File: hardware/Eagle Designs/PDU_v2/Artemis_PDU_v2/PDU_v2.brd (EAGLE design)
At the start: 160 x 100 mm, 101 parts, among them T1 2N5088, U1 DRV8847PWPR, U10 PE014006, U11 IRLML2803PBFCT-ND, U12 IRLML2803PBFCT-ND, U2 DRV8847PWPR, U3 LTC1477CS8LINEAR_TECHNOLOGY_L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, U4 LTC1477CS8LINEAR_TECHNOLOGY_L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, U5 LTC1477CS8LINEAR_TECHNOLOGY_L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, U6 LTC1477CS8LINEAR_TECHNOLOGY_L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, U7 LTC1477CS8LINEAR_TECHNOLOGY_L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, U8 LTC1477CS8LINEAR_TECHNOLOGY_L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, U9 LTC1477CS8LINEAR_TECHNOLOGY_L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

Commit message: updated PDU v2 Eagle files and Artemis Library
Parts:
- added C1, C2: 22uF, HSFL_Main_Library:0805
- added C3, C45, C51: 0.1uF, HSFL_Main_Library:0805
- added C4, C44: 1uF, HSFL_Main_Library:0805
- added C43, C47, C48: 4.7uF, HSFL_Main_Library:0805
- added C46, C49: 10uF, HSFL_Main_Library:0805
- added C50: 0.47uF, HSFL_Main_Library:0805
- added C52: 100pF, HSFL_Main_Library:0805
- added C53: 4.7nF, HSFL_Main_Library:0805
- added C74, C75, C76, C77, C78, C79, C80, C81: 33uF, HSFL_Main_Library:1206
- added D4: (no value), adafruit:SOD-123FL
- added L5: 6uH, HSFL_Main_Library:7443551600
- added M1, M2: BSZ100N06LS3, HSFL_Main_Library:BSZ100N06LS3
- added M3, M4: BSZ033NE2LS5, HSFL_Main_Library:BSZ100N06LS3
- added R1: 4m, HSFL_Main_Library:0805
- added R2: 390K, HSFL_Main_Library:0805
- added R3: 180K, HSFL_Main_Library:0805
- added R30, R32: 10K, HSFL_Main_Library:0805
- added R31: 27K, HSFL_Main_Library:0805
- added R33, R6: 100K, HSFL_Main_Library:0805
- added R4: 15m, HSFL_Main_Library:0805
- added R46: 510K, HSFL_Main_Library:0805
- added R47: 270K, HSFL_Main_Library:0805
- added R5: 130K, HSFL_Main_Library:0805
- added U13: LT8390EFE#PBF, Artemis:SOP65P640X120-29N
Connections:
- new net N$1: C3.1, M1.P$2, M1.P$3, M1.P$4, M2.P$5, M2.P$6, M2.P$7, M2.P$8, M2.P$9, R1.2, U13.3, U13.5
- new net N$2: C3.2, U13.2
- new net N$3: M2.P$1, U13.1
- new net N$38: C52.1, R31.2, U13.20
- new net N$39: C50.1, U13.11, U13.12, U13.13
- new net N$4: M1.P$1, U13.4
- new net N$40: R32.2, R5.1
- new net N$41: C45.1, L5.P$2, M3.P$5, M3.P$6, M3.P$7, M3.P$8, M3.P$9, M4.P$2, M4.P$3, M4.P$4, U13.26
- new net N$42: U13.23
- new net N$43: R6.1, U13.17
- new net N$44: C43.1, R6.2, U13.8
- new net N$45: L5.P$1, R1.1, U13.6
- new net N$47: C45.2, U13.27
- new net N$48: C44.1, C46.1, C49.1, C74.1, C75.1, C76.1, C77.1, M4.P$5, M4.P$6, M4.P$7, M4.P$8, M4.P$9, R4.1, U13.14, U13.24
- new net N$49: M4.P$1, U13.25
- new net N$5: R2.1, R3.2, U13.9
- new net N$50: C51.1, U13.18
- new net N$51: R30.2, R32.1, U13.19
- new net N$52: R33.2, U13.21
- new net N$55: C53.1, R31.1
- new net N$6: M3.P$1, U13.28
- new net V_BATT: C1.1, C2.1, C4.1, C47.1, C48.1, M1.P$5, M1.P$6, M1.P$7, M1.P$8, M1.P$9, R2.2, U13.7
- new net V_BATT_SENSE: R46.2, R47.2
- net GND: now also C1.2, C2.2, C4.2, C43.2, C44.2, C46.2, C47.2, C48.2, C49.2, C50.2, C51.2, C52.2, C53.2, C74.2, C75.2, C76.2, C77.2, C78.2, C79.2, C80.2, C81.2, M2.P$2, M2.P$3, M2.P$4, M3.P$2, M3.P$3, M3.P$4, R3.1, R30.1, R33.1, R47.1, U13.10, U13.22, U13.29
- net VCC: now also C78.1, C79.1, C80.1, C81.1, D4.A, D4.C, R4.2, R46.1, R5.2, U13.15

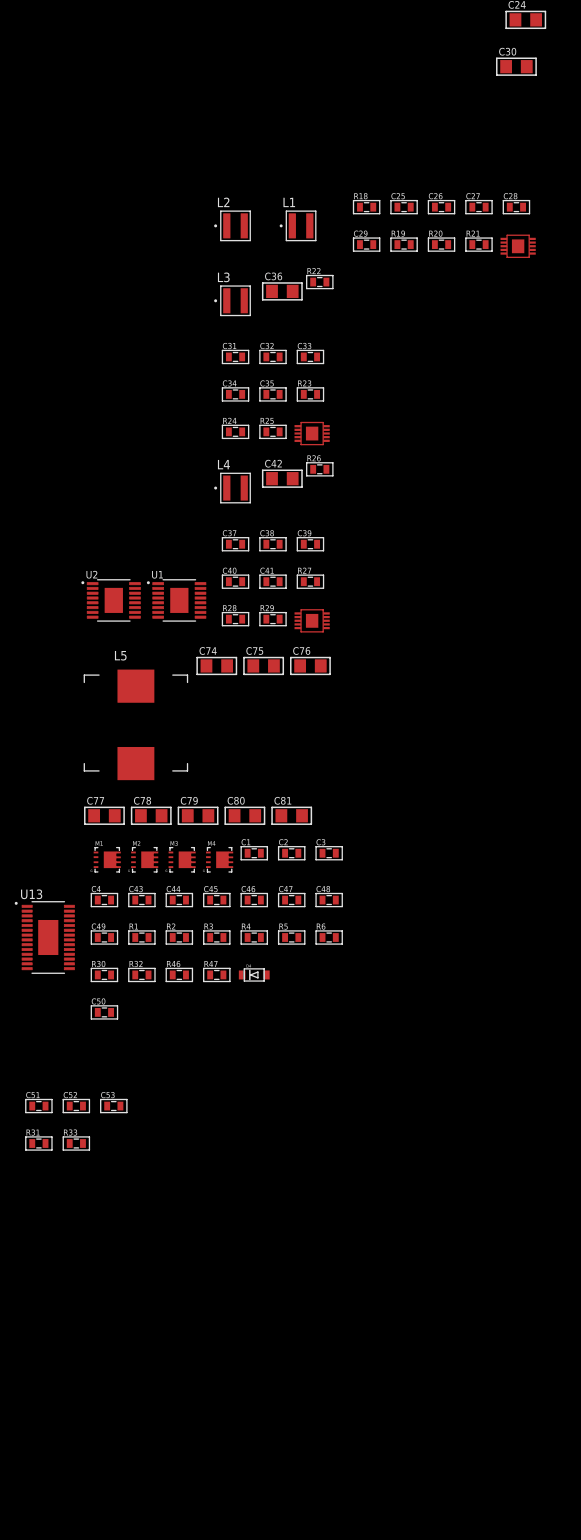
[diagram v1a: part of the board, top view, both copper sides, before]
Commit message: updated PDU v2 H Bridge Circuit Design
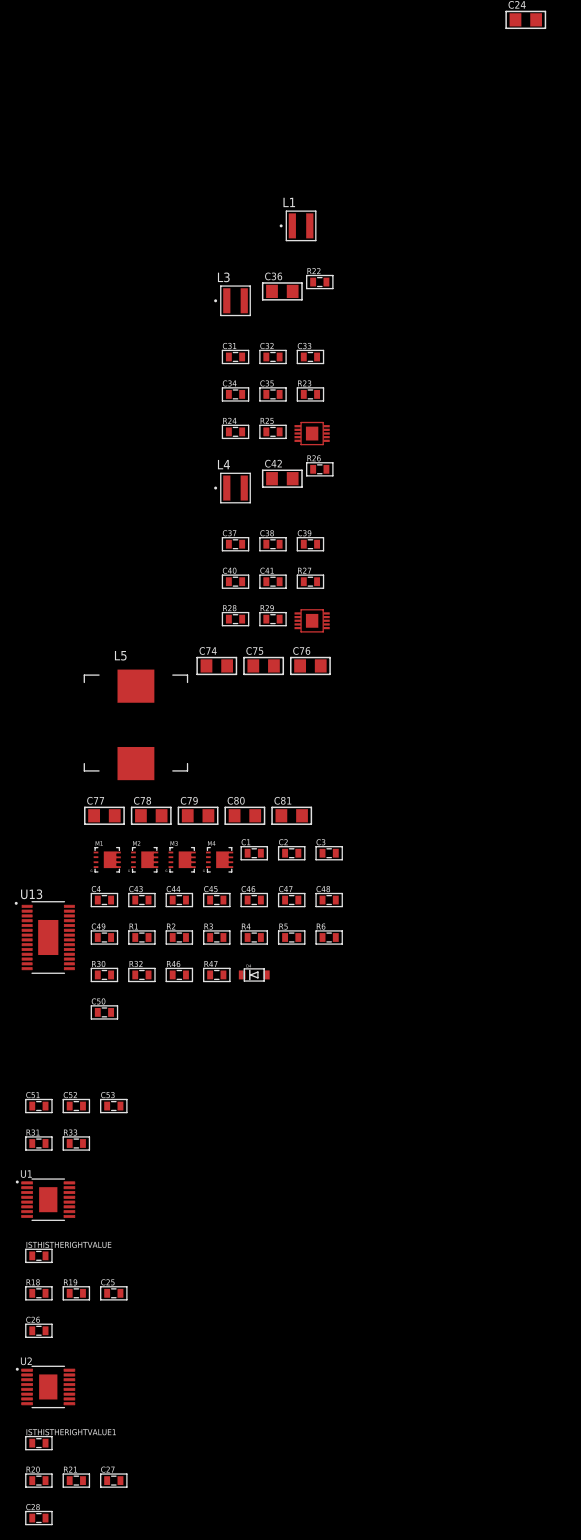
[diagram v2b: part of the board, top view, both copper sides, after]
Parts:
- removed C29: 10 pF, HSFL_Main_Library:0805
- removed C30: 22 uF, HSFL_Main_Library:1206
- removed L2: 2.2 uH, Artemis:IND_XFL4020-222ME
- removed U$4: LT8609A, Artemis:MSOP_10PAD
- added ISTHISTHERIGHTVALUE, ISTHISTHERIGHTVALUE1: 3.3k, HSFL_Main_Library:0805
- C25: value 10 nF -> 0.1 uF
- C26: value 1 uF -> 10 uF
- C28: value 4.7 uF -> 10 uF
- R18: value 18.2 K -> 330 mΩ
- R19: value 187 K -> 330 mΩ
- R20: value 100 K -> 330 mΩ
- R21: value 1 M -> 330 mΩ
- moved C28 189.2 mm to (-268.0, -985.5)
- moved C27 179.7 mm to (-257.8, -980.4)
- moved R20 176.3 mm to (-268.0, -980.4)
- moved R21 176.3 mm to (-262.9, -980.4)
- moved C26 161.9 mm to (-268.0, -960.1)
- moved R18 153.9 mm to (-268.0, -955.0)
- moved C25 152.5 mm to (-257.8, -955.0)
- moved R19 149.0 mm to (-262.9, -955.0)
- moved U2 107.0 mm to (-266.7, -967.7)
- moved U1 83.2 mm to (-266.7, -942.3)
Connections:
- removed net BUS_VBATT_EN: U$4.EN/UV
- removed net PG_VBATT_BUS: R20.1, U$4.PG
- removed net SW_3V3: C6.1, C9.1, U3.1, U3.8, U4.1, U4.8
- removed net SW_3V3_EN: U3.4, U4.4
- removed net SW_5V: C11.1, C13.1, C15.1, C17.1, U5.1, U5.8, U6.1, U6.8, U7.1, U7.8, U8.1, U8.8
- removed net SW_5V_EN: U5.4, U6.4, U7.4, U8.4
- new net 12V_OUT: D4.C, R46.1
- new net HB1_FAULT: ISTHISTHERIGHTVALUE.1, U1.8
- new net HB1_IN1: U1.16
- new net HB1_IN2: U1.15
- new net HB1_IN3: U1.9
- new net HB1_IN4: U1.10
- new net HB1_NSLEEP: U1.1
- new net HB1_OUT1: U1.2
- new net HB1_OUT2: U1.4
- new net HB1_OUT3: U1.7
- new net HB1_OUT4: U1.5
- new net HB1_TRQ: U1.11
- new net HB2_FAULT: ISTHISTHERIGHTVALUE1.1, U2.8
- new net HB2_IN1: U2.16
- new net HB2_IN2: U2.15
- new net HB2_IN3: U2.9
- new net HB2_IN4: U2.10
- new net HB2_NSLEEP: U2.1
- new net HB2_OUT1: U2.2
- new net HB2_OUT2: U2.4
- new net HB2_OUT3: U2.7
- new net HB2_OUT4: U2.5
- new net HB2_TRQ: U2.11
- new net NAMETHIS: C25.2, C26.2, C27.2, C28.2, U1.12, U2.12
- new net NAMETHIS__: ISTHISTHERIGHTVALUE.2, ISTHISTHERIGHTVALUE1.2
- new net SW_3V3_1: C6.1, U3.1, U3.8
- new net SW_3V3_2: C9.1, U4.1, U4.8
- new net SW_3V3_EN_1: U3.4
- new net SW_3V3_EN_2: U4.4
- new net SW_5V_1: C11.1, U5.1, U5.8
- new net SW_5V_2: C13.1, U6.1, U6.8
- new net SW_5V_3: C15.1, U7.1, U7.8
- new net SW_5V_4: C17.1, U8.1, U8.8
- new net SW_5V_EN_1: U5.4
- new net SW_5V_EN_2: U6.4
- new net SW_5V_EN_3: U7.4
- new net SW_5V_EN_4: U8.4
- net BUS_VBATT: no longer C29.2, C30.1, L2.2, R20.2, R21.2
- net GND: now also R20.1, R21.1; no longer C25.2, C26.2, C28.2, C30.2, U$4.GND, U$4.SYNC, U1.13, U2.13
- net N$19: now also C27.1, C28.1, U2.13; no longer R18.2, U$4.RT
- net N$20: now also C26.1, U1.13; no longer U$4.TR/SS
- net N$21: now also R19.2, U1.6; no longer C26.1, U$4.INTVCC
- net N$22: now also R18.2, U1.3; no longer C27.1, U$4.BST
- net N$23: now also R21.2, U2.6; no longer C27.2, L2.1, U$4.SW
- net N$24: now also R20.2, U2.3; no longer C29.1, R19.2, R21.1, U$4.FB
- net PCM_VBATT: no longer C28.1, U$4.VIN
- net VCC: no longer D4.C, R46.1

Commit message: updated PDU v2 and Artemis Library
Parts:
- removed U$10, U$11, U$12, U$13, U$14, U$17, U$18, U$19, U$20, U$21, U$8, U$9: MOLEX_5037630291, Artemis:5037630291
- removed U$15, U$16: NDS8434, Artemis:SO08
- added C29, C59, C60, C61: 0.1 uF, HSFL_Main_Library:0805
- added C30, C62, C63: (no value), HSFL_Main_Library:0805
- added C54, C56: 10 uF, HSFL_Main_Library:0805
- added C55, C57, C58: 1 uF, HSFL_Main_Library:0805
- added J1, J10, J11, J12, J13, J14, J16, J17, J18, J19, J2, J3, J4, J5, J6, J7, J8, J9: 5037630291, Artemis:CON_5037630291
- added J15: 5037630491, Artemis:CON_5037630491
- added R34: 3.3k, HSFL_Main_Library:0805
- added R35: 2m, HSFL_Main_Library:0805
- added R36: 3.3k, HSFL_Main_Library:0603-RES
- added R37: 10 uH, Artemis:RESC0805X60N
- added R38: 10k, HSFL_Main_Library:0805
- added R39: 316k, HSFL_Main_Library:0805
- added R40: 110k, HSFL_Main_Library:0805
- added U$2, U$4: TEST_POINT, HSFL_Main_Library:TEST_POINT
- added U14: ATSAMD51J19A-AU, Artemis:TQFP64_PT_MCH
- added U15: INA219BIDR, Artemis:SOIC127P599X175-8N
- added Y1: ABS07-32.768KHZ-T, Artemis:XTAL_ABS07-32.768KHZ-T
- U$6, U$7: value MOLEX_5037630291 -> NDS8434; device Artemis:5037630291 -> Artemis:SO08
- moved R24 1487.4 mm to (-268.0, 649.0)
- moved R25 1487.4 mm to (-262.9, 649.0)
- moved U$5 1487.4 mm to (-259.1, 650.2)
- moved C34 1477.3 mm to (-268.0, 643.9)
- moved C35 1477.3 mm to (-262.9, 643.9)
- moved R23 1477.3 mm to (-257.8, 643.9)
- moved C31 1467.1 mm to (-268.0, 638.8)
- moved C32 1467.1 mm to (-262.9, 638.8)
- moved C33 1467.1 mm to (-257.8, 638.8)
- moved L3 1451.9 mm to (-268.0, 631.2)
- moved C36 1449.3 mm to (-261.6, 629.9)
- moved R22 1448.0 mm to (-256.5, 629.9)
- moved U$6 1063.5 mm to (-287.0, -1455.4)
- moved U$7 1055.3 mm to (-292.1, -1455.4)
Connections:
- net HB1_OUT1 renamed TORQUE_1A
- net HB1_OUT2 renamed TORQUE_1B
- net HB1_OUT3 renamed TORQUE_2A
- net HB1_OUT4 renamed TORQUE_2B
- net HB2_OUT1 renamed TORQUE_3A
- net HB2_OUT2 renamed TORQUE_3B
- net HB2_OUT3 renamed TORQUE_4A
- net HB2_OUT4 renamed TORQUE_4B
- removed net 5V_SW1: U$10.1, U$11.1, U$6.1, U$7.1, U$8.1, U$9.1
- removed net VSOLAR: U$14.2, U$17.2, U$18.2, U$19.2, U$20.2, U$21.2
- new net +3V3: R38.2
- new net 3V3_SW1: J15.1
- new net 5V_SW4: J15.2
- new net BAT_CHARGE: J17.1
- new net BAT_IN: J16.1
- new net INH_SW1_COM: J18.2
- new net INH_SW1_NC: J18.1
- new net INH_SW3_COM: J19.2
- new net INH_SW3_NC: J19.1
- new net N$46: R37.2, U14.55
- new net N$54: C61.1, R39.1, R40.1, U14.15
- new net N$56: U$2.1, U15.2
- new net N$57: U$4.1, U15.1
- new net N$58: C54.1, C55.1, R37.1, U14.53
- new net N$59: R34.2, U15.3
- new net N$60: C62.2, U14.1, Y1.2
- new net N$61: R36.2, U15.4
- new net N$62: C63.2, U14.2, Y1.1
- new net SOLAR_IN1: J1.1, J7.2
- new net SOLAR_IN2: J2.1, J8.2
- new net SOLAR_IN3: J3.1, J9.2
- new net SOLAR_IN4: J10.2, J4.1
- new net SOLAR_IN5: J11.2, J5.1
- new net SOLAR_IN6: J12.2, J6.1
- new net VS: C29.1, R34.1, R36.1, U15.5
- net GND: now also C29.2, C54.2, C55.2, C56.1, C56.2, C57.1, C57.2, C58.1, C58.2, C59.1, C59.2, C60.1, C60.2, C61.2, C62.1, C63.1, J1.2, J1.3, J1.4, J10.1, J10.3, J10.4, J11.1, J11.3, J11.4, J12.1, J12.3, J12.4, J13.1, J13.3, J13.4, J14.1, J14.3, J14.4, J15.3, J15.4, J15.5, J15.6, J16.2, J16.3, J16.4, J17.2, J17.3, J17.4, J18.3, J18.4, J19.3, J19.4, J2.2, J2.3, J2.4, J3.2, J3.3, J3.4, J4.2, J4.3, J4.4, J5.2, J5.3, J5.4, J6.2, J6.3, J6.4, J7.1, J7.3, J7.4, J8.1, J8.3, J8.4, J9.1, J9.3, J9.4, R35.2, R38.1, R40.2, U14.21, U14.22, U14.33, U14.34, U14.47, U14.48, U14.54, U14.56, U14.7, U14.8, U15.6, U15.7; no longer U$10.2, U$11.2, U$12.1, U$13.1, U$14.1, U$17.1, U$18.1, U$19.1, U$20.1, U$21.1, U$6.2, U$7.2, U$8.2, U$9.2
- net N$13: now also U$6.1, U$6.2, U$6.3, U$7.1, U$7.2, U$7.3; no longer U$15.1, U$15.2, U$15.3, U$16.1, U$16.2, U$16.3
- net N$15: now also U$7.4; no longer U$16.4
- net N$18: now also U$6.4; no longer U$15.4
- net VBATT: now also R39.2
- net VBURN1: now also J13.2, U$6.5, U$6.6, U$6.7, U$6.8; no longer U$12.2, U$15.5, U$15.6, U$15.7, U$15.8
- net VBURN2: now also J14.2, U$7.5, U$7.6, U$7.7, U$7.8; no longer U$13.2, U$16.5, U$16.6, U$16.7, U$16.8
- net VCC: now also R35.1, U15.8
